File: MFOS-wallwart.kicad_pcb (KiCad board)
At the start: 2 copper layers, 125 x 65 mm, 32 parts, among them J1 Barrel_Jack, J2 , J3 Conn_02x05_Odd_Even, SW1 SW_SPST, U1 L7812, U2 L7912, U3 L7805

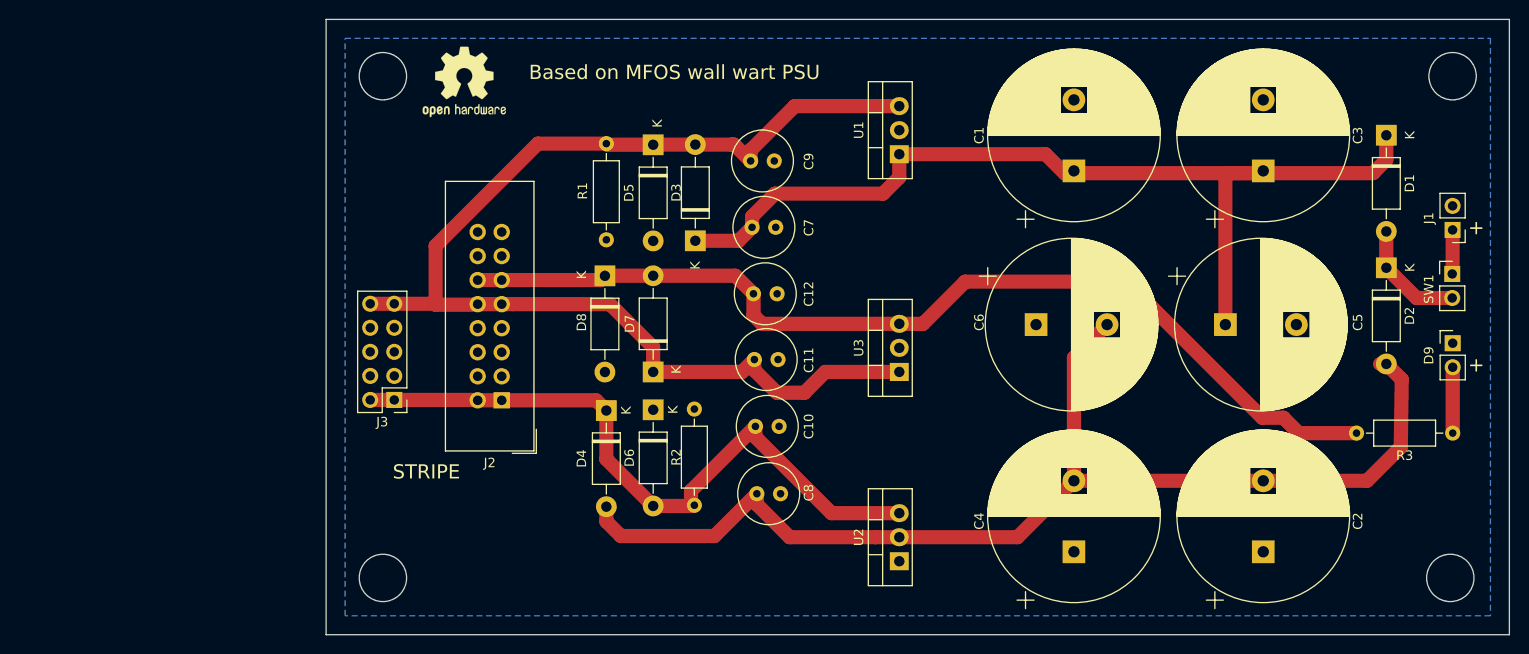
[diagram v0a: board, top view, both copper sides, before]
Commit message: Updated for extra outputs
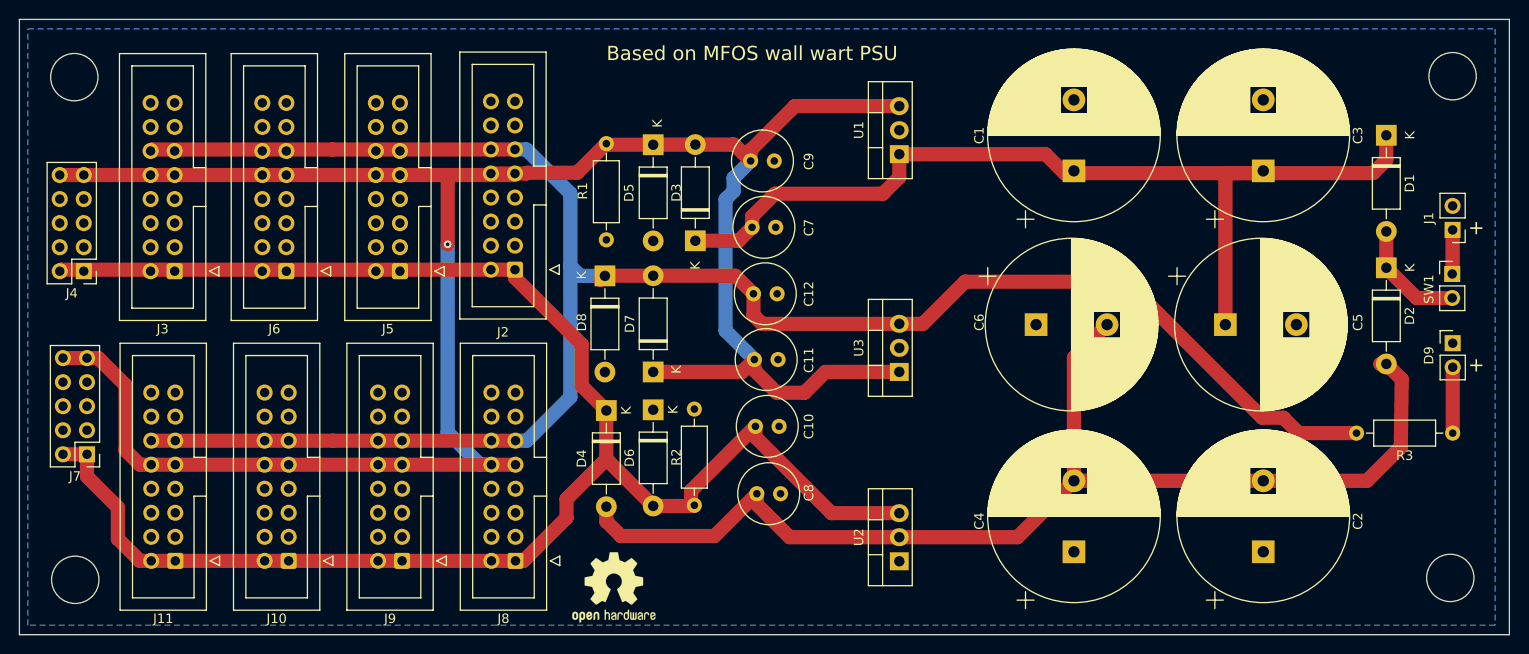
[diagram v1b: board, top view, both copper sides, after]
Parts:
- added J10: Connector_Generic:Conn_02x08_Odd_Even, Connector_IDC:IDC-Header_2x08_P2.54mm_Vertical, F.Cu at (81.0, 112.2)
- added J11: Connector_Generic:Conn_02x08_Odd_Even, Connector_IDC:IDC-Header_2x08_P2.54mm_Vertical, F.Cu at (69.1, 112.2)
- added J4: Conn_02x05_Odd_Even, Connector_PinHeader_2.54mm:PinHeader_2x05_P2.54mm_Vertical, F.Cu at (59.4, 81.6)
- added J5: Connector_Generic:Conn_02x08_Odd_Even, Connector_IDC:IDC-Header_2x08_P2.54mm_Vertical, F.Cu at (92.8, 81.6)
- added J6: Connector_Generic:Conn_02x08_Odd_Even, Connector_IDC:IDC-Header_2x08_P2.54mm_Vertical, F.Cu at (80.8, 81.6)
- added J7: Conn_02x05_Odd_Even, Connector_PinHeader_2.54mm:PinHeader_2x05_P2.54mm_Vertical, F.Cu at (59.7, 100.9)
- added J8: Connector_Generic:Conn_02x08_Odd_Even, Connector_IDC:IDC-Header_2x08_P2.54mm_Vertical, F.Cu at (105.0, 112.2)
- added J9: Connector_Generic:Conn_02x08_Odd_Even, Connector_IDC:IDC-Header_2x08_P2.54mm_Vertical, F.Cu at (93.0, 112.2)
- J2: value (none) -> Connector_Generic:Conn_02x08_Odd_Even
- J3: value Conn_02x05_Odd_Even -> Connector_Generic:Conn_02x08_Odd_Even; footprint Connector_PinHeader_2.54mm:PinHeader_2x05_P2.54mm_Vertical -> Connector_IDC:IDC-Header_2x08_P2.54mm_Vertical
- moved REF** 55.7 mm to (115.4, 115.0)
- moved J3 26.9 mm to (69.0, 81.6)
- moved J2 13.9 mm to (105.0, 81.4)
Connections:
- J2 pad 13: Net-(J2-Pad13) -> (no net)
- J2 pad 14: Net-(J2-Pad14) -> (no net)
- J2 pad 15: Net-(J2-Pad15) -> (no net)
- J2 pad 16: Net-(J2-Pad16) -> (no net)
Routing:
- net -12V: track 73.0 -> 185.7 mm
- net +12V: track 127.5 -> 239.1 mm, vias 0 -> 1
- net +5V: track 105.2 -> 210.3 mm
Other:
- board size 125 x 65 mm -> 157.4 x 65 mm
- board text removed: "STRIPE"

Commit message: Minor updates, add polarity to 1uf caps
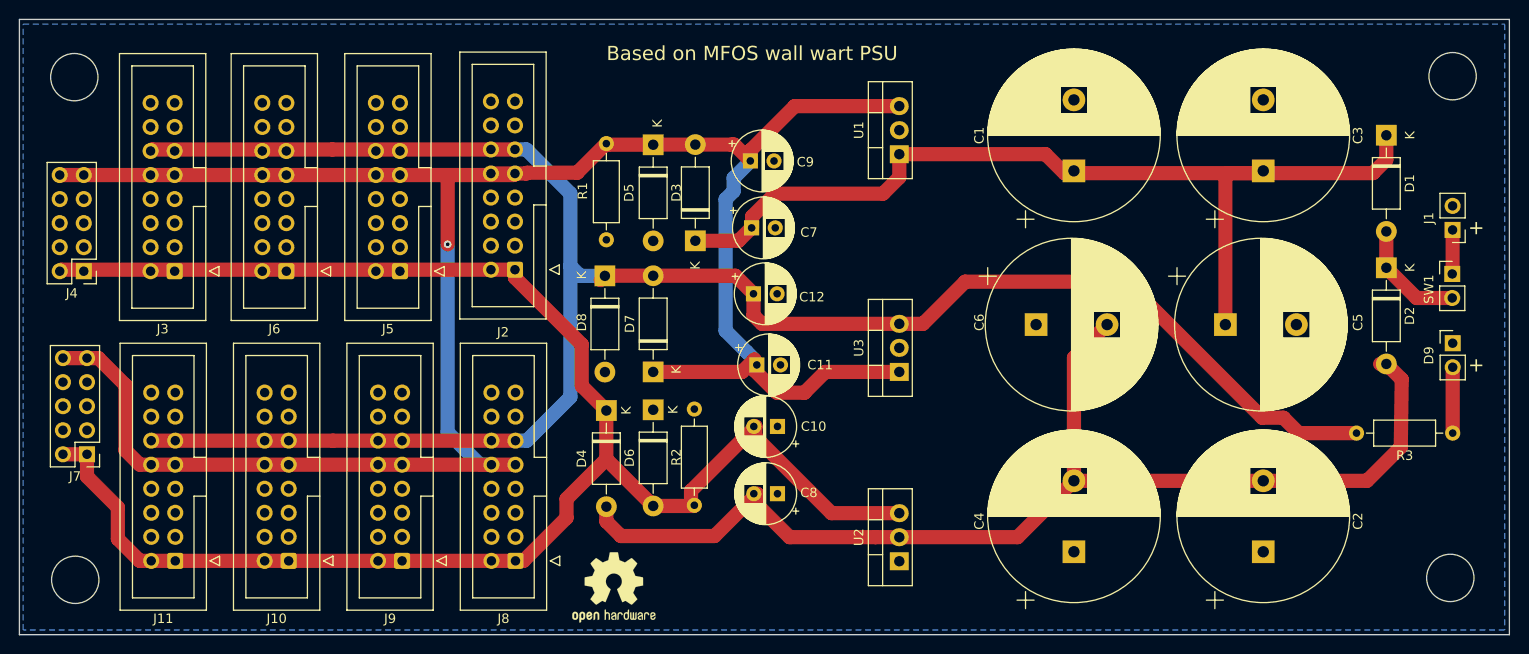
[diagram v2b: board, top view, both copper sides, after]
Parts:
- C10, C11, C12, C7, C8, C9: footprint Capacitor_THT:C_Radial_D6.3mm_H5.0mm_P2.50mm -> Capacitor_THT:CP_Radial_D6.3mm_P2.50mm
- moved C10 2.33 mm to (132.7, 98.0), turned to 180 degrees
- moved C11 2.31 mm to (130.5, 91.5), turned to 0 degrees
- moved C8 2.18 mm to (132.7, 105.1), turned to 180 degrees
- moved C7 0.08 mm to (129.9, 77.0)
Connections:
- C10 pad 1: -12V -> GND
- C10 pad 2: GND -> -12V
- C11 pad 1: GND -> +12V
- C11 pad 2: +12V -> GND
- C8 pad 1: Net-(C2-Pad2) -> GND
- C8 pad 2: GND -> Net-(C2-Pad2)
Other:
- net class Default removed
